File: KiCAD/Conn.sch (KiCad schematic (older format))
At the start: 0 parts

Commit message: completed 5V buck schematic and setup
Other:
- note added: "AIN and Hall effects"
- note added: "Extra I/O"
- note added: "Pwr Screw Terms\n"
- note added: "Shiftbutton Screw Terms"
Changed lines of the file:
@@
 LIBS:contrib
 LIBS:valves
+LIBS:TPS565208
 LIBS:OBC-PDB-cache
 EELAYER 25 0
@@
 $Descr A4 11693 8268
 encoding utf-8
-Sheet 1 6
+Sheet 4 6
 Title ""
 Date ""
@@
 Comment4 ""
 $EndDescr
+Text Notes 3900 1300 0    118  ~ 0
+Pwr Screw Terms\n
+Text Notes 9300 2550 0    118  ~ 0
+Extra I/O
+Text Notes 4850 5300 0    118  ~ 0
+AIN and Hall effects
+Text Notes 2500 3850 0    118  ~ 0
+Shiftbutton Screw Terms
 $EndSCHEMATC

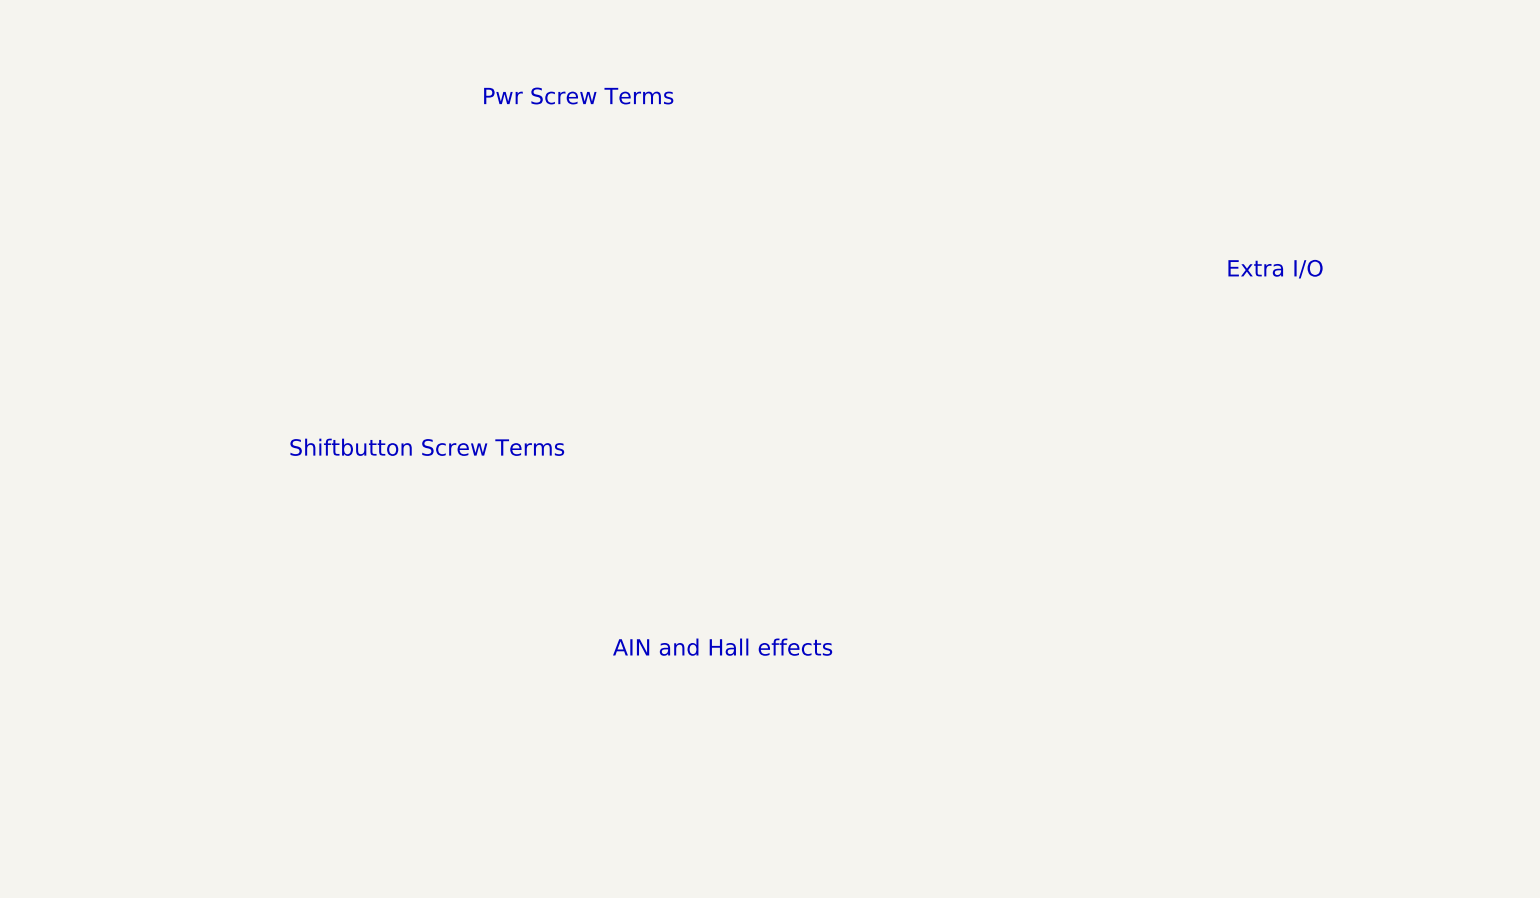
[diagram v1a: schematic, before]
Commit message: µC ATMEGA2560 added and pins labeled, w/ supp components
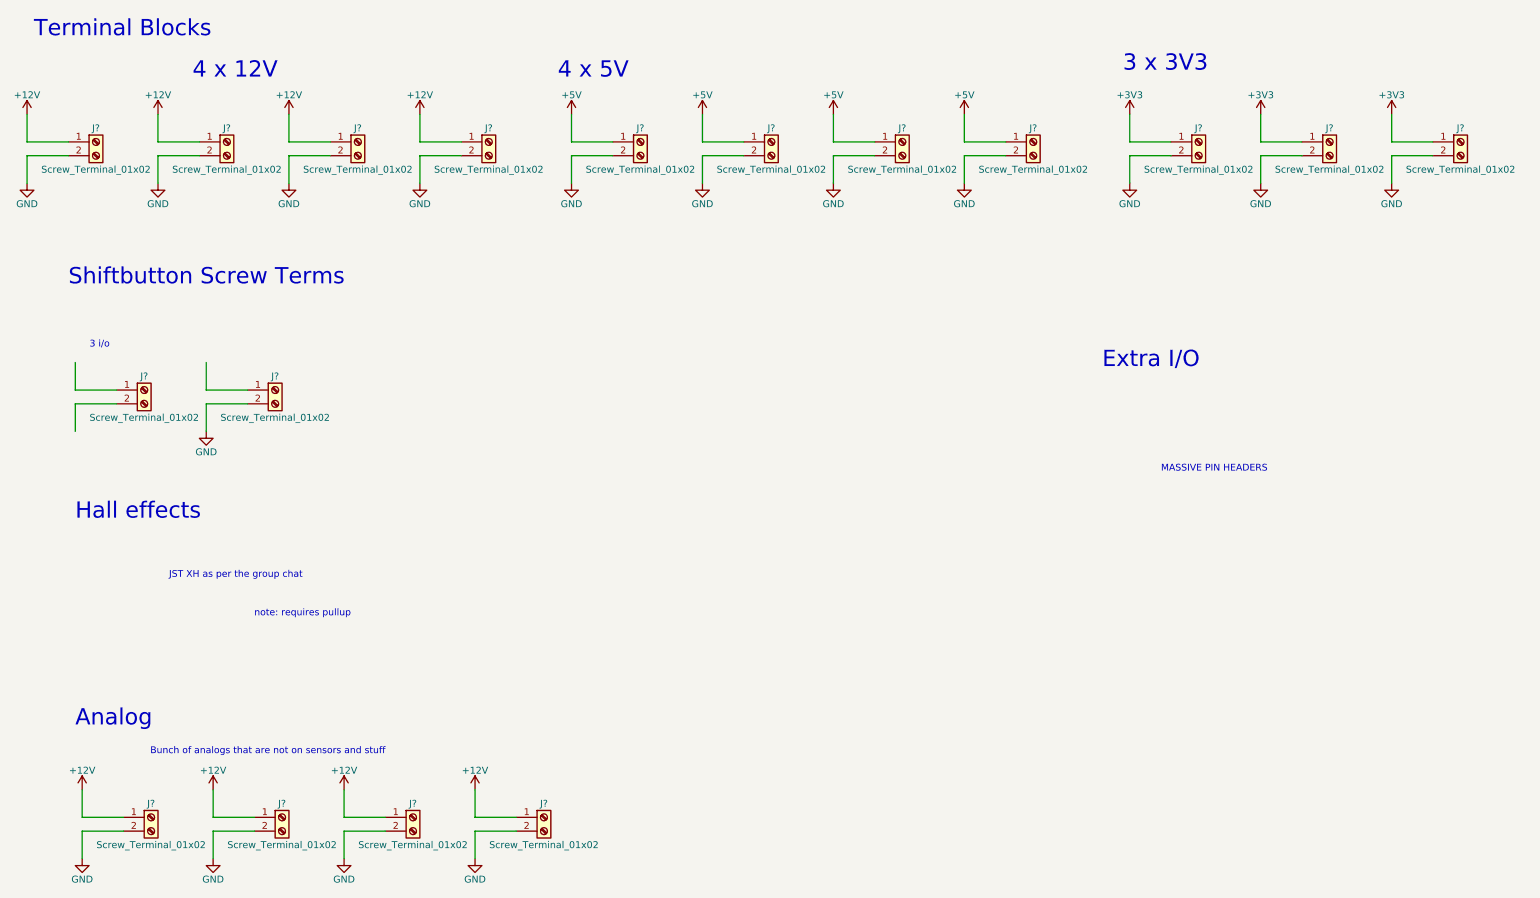
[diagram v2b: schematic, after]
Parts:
- added J? (x17): Screw_Terminal_01x02, TerminalBlock:TerminalBlock_bornier-2_P5.08mm, symbol Screw_Terminal_01x02
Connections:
- net labels added: +12V, +3V3, +5V, GND
- wire segments 0 -> 68
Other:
- note added: "3 i/o\n"
- note added: "3 x 3V3\n"
- note added: "4 x 12V"
- note added: "4 x 5V"
- note added: "Analog"
- note added: "Bunch of analogs that are not on sensors and stuff"
- note added: "Hall effects"
- note added: "JST XH as per the group chat \n\n"
- note added: "MASSIVE PIN HEADERS\n"
- note added: "Terminal Blocks\n"
- note added: "note: requires pullup"
- note removed: "AIN and Hall effects"
- note removed: "Pwr Screw Terms\n"

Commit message: Schematic small fix
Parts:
- removed J? (x3): Screw_Terminal_01x02, TerminalBlock:TerminalBlock_bornier-2_P5.08mm, symbol Screw_Terminal_01x02
- added Hall1, Hall2, Hall3, Hall4, Hall5, Hall6: Conn_01x03, Connectors_JST:JST_XH_B03B-XH-A_03x2.50mm_Straight, symbol Conn_01x03
- added I2C1, I2C2, I2C3: Conn_01x04, Pin_Headers:Pin_Header_Straight_1x04_Pitch2.54mm, symbol Conn_01x04
- added J11, J13, J4: Screw_Terminal_01x02, TerminalBlock:TerminalBlock_bornier-2_P5.08mm, symbol Screw_Terminal_01x02
- added J18: Conn_02x20_Top_Bottom, symbol Conn_02x20_Top_Bottom
- added R10, R11, R12, R13, R14, R15: 10k, Resistors_SMD:R_0805, symbol R
- added SPI1, SPI2, SPI3: Conn_01x06, Pin_Headers:Pin_Header_Straight_1x06_Pitch2.54mm, symbol Conn_01x06
- added U4: Si8660, Housings_SOIC:SOIC-16W_5.3x10.2mm_Pitch1.27mm, symbol Si8660
- gave numbers to parts that had none: 14
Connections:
- net labels added: 20(SDA), 21(SCL), 50(MISO), 51(MOSI), 52(SCK), 53(SS), Earth_Protective, Hall1, Hall2, Hall3, Hall4, Hall5, Hall6, digiXX?
- wire segments 68 -> 151
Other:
- note added: "3 Shift Buttons\n"
- note added: "Buttons"
- note added: "I2C and SPI\n"
- note added: "Remaining Pins (Male)"
- note removed: "3 i/o\n"
- note removed: "JST XH as per the group chat \n\n"
- note removed: "MASSIVE PIN HEADERS\n"
- note removed: "note: requires pullup"
- moved on the sheet: J5, J7, J8

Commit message: transfer for mechanical step
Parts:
- J18: footprint (none) -> Pin_Headers:Pin_Header_Straight_2x20_Pitch2.54mm
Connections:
- net labels added: 22, 23, 31, 32, 33, 38, 40, 41, A10, A11, A12, A13, A14, A15, A9
- net labels removed: 53(SS), digiXX?
- wire segments 151 -> 157
